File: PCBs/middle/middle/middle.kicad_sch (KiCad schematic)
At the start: 28 parts, among them J15 Screw_Terminal_01x02, J16 Screw_Terminal_01x02, J17 Screw_Terminal_01x02, J18 Screw_Terminal_01x02, J19 Screw_Terminal_01x02, J2 Screw_Terminal_01x03, J21 Screw_Terminal_01x02, J3 Screw_Terminal_01x03, J4 Screw_Terminal_01x03, J5 Screw_Terminal_01x03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

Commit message: FINAL?
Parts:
- F1: footprint Fuse:Fuseholder_Clip-5x20mm_Schurter_OG_Lateral_P15.00x5.00mm_D1.3mm_Horizontal -> Fuse:Fuseholder_Clip-5x20mm_Littelfuse_520_Inline_P20.50x5.80mm_D1.30mm_Horizontal
- R1, R2: footprint Resistor_THT:R_Axial_DIN0204_L3.6mm_D1.6mm_P5.08mm_Horizontal -> Resistor_THT:R_Axial_DIN0207_L6.3mm_D2.5mm_P10.16mm_Horizontal
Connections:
- net CE: now also U1.34 (RX8), U3.3 (CE); no longer U1.35 (TX8), U3.8 (IRQ)
- net IRQ: now also U1.35 (TX8), U3.8 (IRQ); no longer U1.34 (RX8), U3.3 (CE)
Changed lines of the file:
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@@
 		)
 	)
-	(label "CE"
+	(label "IRQ"
 		(at 224.79 146.05 180)
 		(effects
@@
 		)
 	)
-	(label "IRQ"
+	(label "CE"
 		(at 224.79 143.51 180)
 		(effects
@@
 		)
 	)
-	(label "IRQ"
+	(label "CE"
 		(at 87.63 80.01 180)
 		(effects
@@
 		)
 	)
-	(label "CE"
+	(label "IRQ"
 		(at 87.63 82.55 180)
 		(effects
@@
 			)
 		)
-		(property "Footprint" "Resistor_THT:R_Axial_DIN0204_L3.6mm_D1.6mm_P5.08mm_Horizontal"
+		(property "Footprint" "Resistor_THT:R_Axial_DIN0207_L6.3mm_D2.5mm_P10.16mm_Horizontal"
 			(at 155.702 134.62 90)
 			(hide yes)
@@
 			)
 		)
-		(property "Footprint" "Fuse:Fuseholder_Clip-5x20mm_Schurter_OG_Lateral_P15.00x5.00mm_D1.3mm_Horizontal"
+		(property "Footprint" "Fuse:Fuseholder_Clip-5x20mm_Littelfuse_520_Inline_P20.50x5.80mm_D1.30mm_Horizontal"
 			(at 156.21 64.008 90)
 			(hide yes)
@@
 			)
 		)
-		(property "Footprint" "Resistor_THT:R_Axial_DIN0204_L3.6mm_D1.6mm_P5.08mm_Horizontal"
+		(property "Footprint" "Resistor_THT:R_Axial_DIN0207_L6.3mm_D2.5mm_P10.16mm_Horizontal"
 			(at 155.702 144.78 90)
 			(hide yes)

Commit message: final
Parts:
- added J1: Conn_01x04_Pin, Connector_PinSocket_2.54mm:PinSocket_1x04_P2.54mm_Vertical, symbol Connector:Conn_01x04_Pin
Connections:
- net +3.3V: now also J1.1 (Pin_1)
- net GND: now also J1.2 (Pin_2)
- net at U1.24 (A10): now also J1.3 (Pin_3)
- net at U1.25 (A11): now also J1.4 (Pin_4)

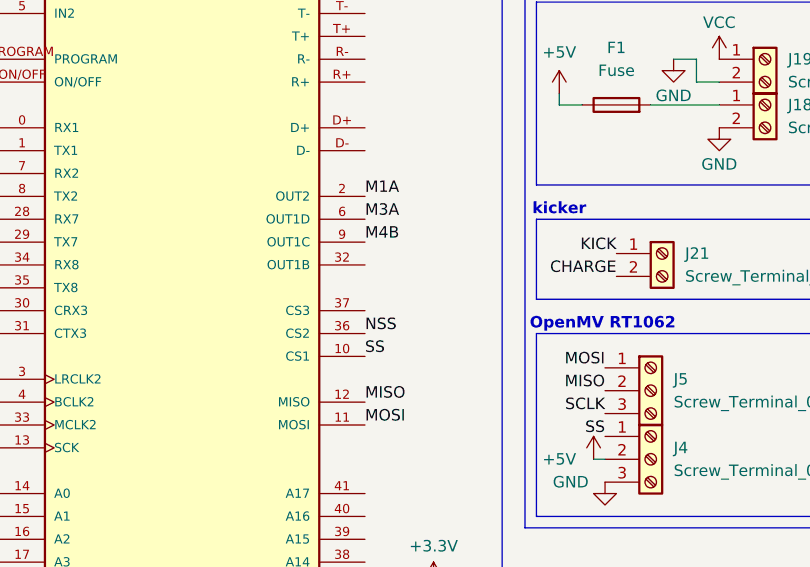
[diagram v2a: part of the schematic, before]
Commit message: final v4 add esc to middle
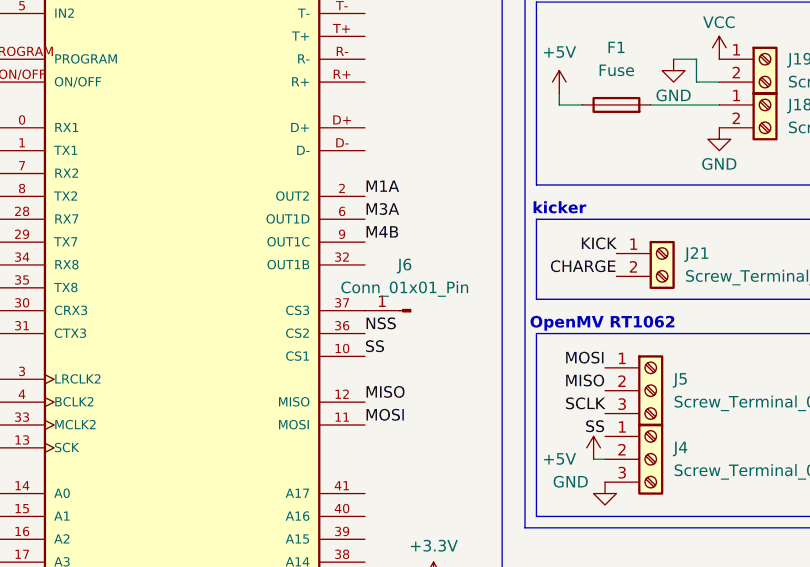
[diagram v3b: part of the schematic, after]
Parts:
- added J6: Conn_01x01_Pin, Connector_PinHeader_2.54mm:PinHeader_1x01_P2.54mm_Vertical, symbol Connector:Conn_01x01_Pin
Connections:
- net at U1.37 (CS3): now also J6.1 (Pin_1)
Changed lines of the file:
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@@
+		)
+	)
+	(symbol
+		(lib_id "Connector:Conn_01x01_Pin")
+		(at 133.35 85.09 0)
+		(mirror y)
+		(unit 1)
+		(body_style 1)
+		(exclude_from_sim no)
+		(in_bom yes)
+		(on_board yes)
+		(in_pos_files yes)
+		(dnp no)
+		(property "Reference" "J6"
+			(at 132.715 80.01 0)
+			(show_name no)
+			(do_not_autoplace no)
+			(effects
+				(font
+					(size 1.27 1.27)
+				)
+			)
+		)
+		(property "Value" "Conn_01x01_Pin"
+			(at 132.715 82.55 0)
+			(show_name no)
+			(do_not_autoplace no)
+			(effects
+				(font
+					(size 1.27 1.27)
+				)
+			)
+		)
+		(property "Footprint" "Connector_PinHeader_2.54mm:PinHeader_1x01_P2.54mm_Vertical"
+			(at 133.35 85.09 0)
+			(hide yes)
+			(show_name no)
+			(do_not_autoplace no)
+			(effects
+				(font
+					(size 1.27 1.27)
+				)
+			)
+		)
+		(property "Datasheet" ""
+			(at 133.35 85.09 0)
+			(hide yes)
+			(show_name no)
+			(do_not_autoplace no)
+			(effects
+				(font
+					(size 1.27 1.27)
+				)
+			)
+		)
+		(property "Description" "Generic connector, single row, 01x01, script generated"
+			(at 133.35 85.09 0)
+			(hide yes)
+			(show_name no)
+			(do_not_autoplace no)
+			(effects
+				(font
+					(size 1.27 1.27)
+				)
+			)
+		)
+		(pin "1"
+		)
+		(instances
+			(project "middle"
+				(path "/a4715291-ecb7-4f51-bcfc-c96d25ee48c5"
+					(reference "J6")
+					(unit 1)
+				)
+			)
 		)
 	)
